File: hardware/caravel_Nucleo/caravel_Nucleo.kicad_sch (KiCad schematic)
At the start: 88 parts, among them J1 USB4105-GF-A, J10 PinHeader_1x11, J11 PinHeader_1x02, J12 PinHeader_1x02, J2 M20-9990246, J3 PinHeader_1x02, J4 61300411121, J5 PinHeader_1x02, J6 PinHeader_1x02, J7 61300611121, J8 640456-3, J9 640456-3, Q1 BSS84AKW, SW1 KMR2, T1 Logo, T2 Logo, U1 FT232HQ, U12 NUCLEO144-F429ZI, U2 SN74LVC1G125DCKR, U3 SN74LVC1G125DCKR, U4 MAX811REUS+T, U5 MCP4661-103E/ML, U6 Caravel_breakout_PCB, U7 W25Q32FVSS, U9 MIC2211-AAYML-TR, X1 ECS-2520MVLC-100-BN-TR, Y1 ABM8G-12.000MHZ-18-D2Y-T

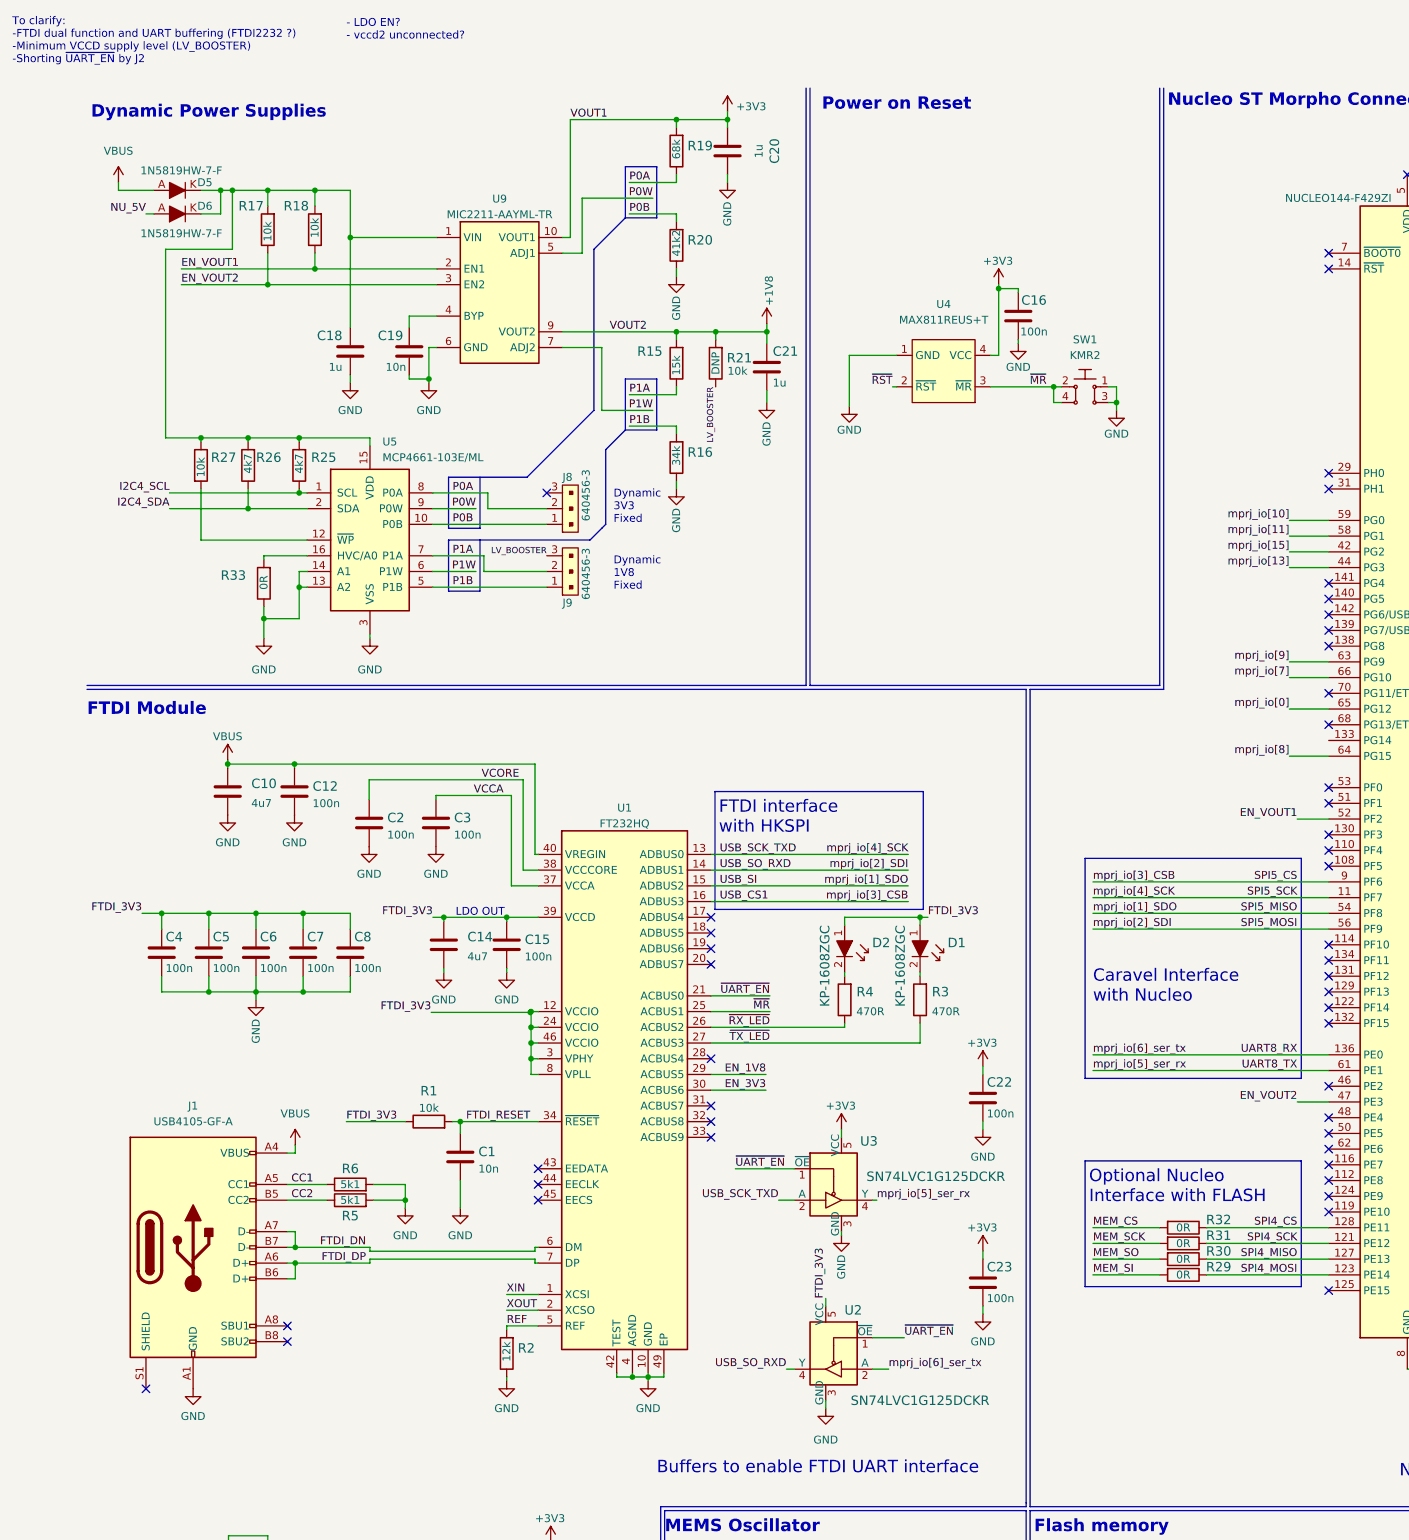
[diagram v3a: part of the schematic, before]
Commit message: Add UART_EN signal short protection for FTDI, add OR gate for enabling LDO
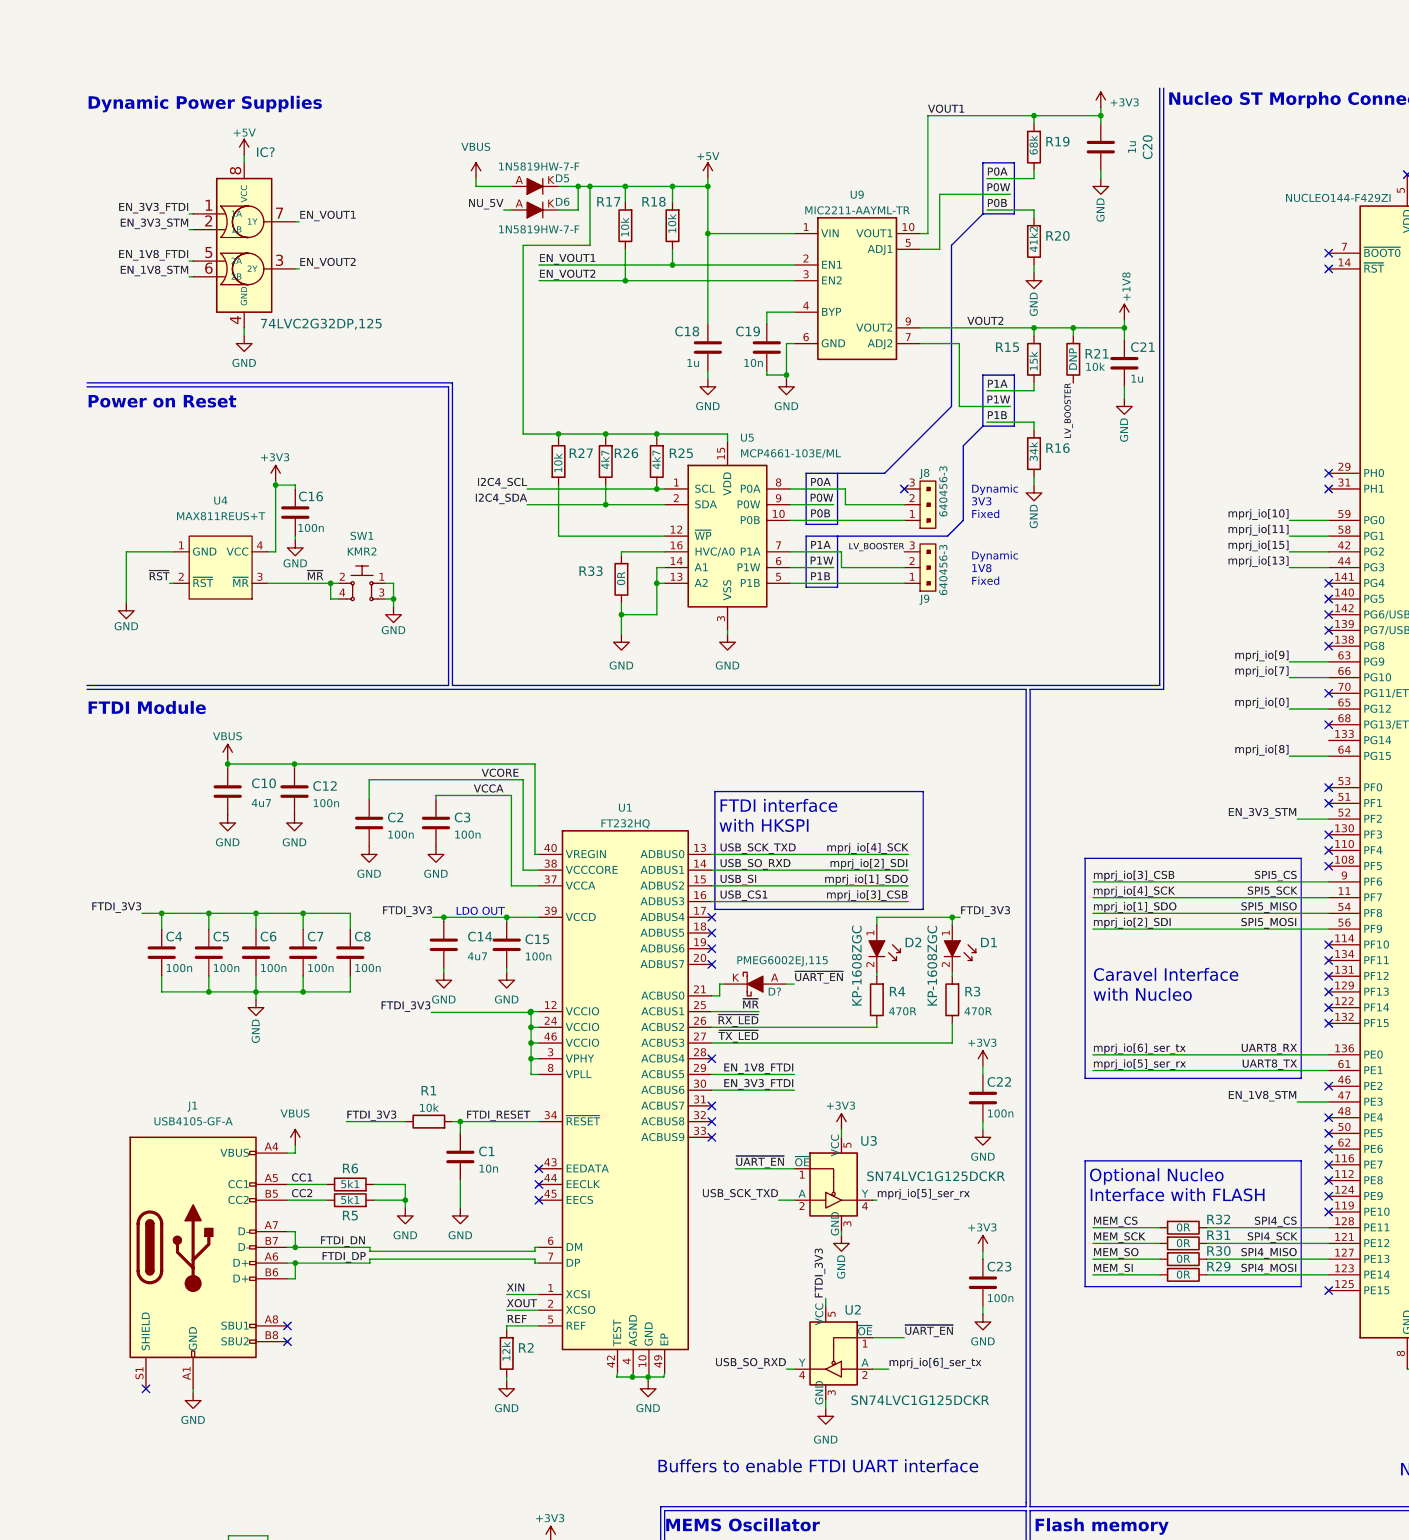
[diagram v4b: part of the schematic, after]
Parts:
- added D?: PMEG6002EJ,115, antmicro-footprints:SOD-323F, symbol antmicroDiodesRectifiersSingle:PMEG6002EJ,115
- added IC?: 74LVC2G32DP,125, antmicro-footprints:TSSOP-8_W3mm, symbol antmicroLogicGatesandInverters:74LVC2G32DP,125
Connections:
- net +5V: now also C18.1, D5.K, D6.K, R17.2, R18.2, R25.2, R26.2, R27.1, U5.15 (VDD), U9.1 (VIN), IC?.8 (VCC)
- net AGND: now also IC?.4 (GND)
- net EN_VOUT1: now also IC?.7 (1Y); no longer U12.52 (PF2)
- net EN_VOUT2: now also IC?.3 (2Y); no longer U12.47 (PE3)
- net ~{UART_EN}: now also D?.A; no longer U1.21 (ACBUS0)
- net EN_1V8 renamed EN_1V8_FTDI
- net EN_1V8_FTDI: now also IC?.5 (2A)
- net EN_3V3 renamed EN_3V3_FTDI
- net EN_3V3_FTDI: now also IC?.1 (1A)
- new net: D?.K, U1.21 (ACBUS0)
- new net EN_1V8_STM: IC?.6 (2B), U12.47 (PE3)
- new net EN_3V3_STM: IC?.2 (1B), U12.52 (PF2)
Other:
- note removed: "- LDO EN? - vccd2 unconnected?"
- note removed: "To clarify: -FTDI dual function and UART buffering (FTDI2232 ?) -Minimum VCCD supply level (LV_BOOSTER) -Shorting ~{UART_EN} by J2"
- moved on the sheet: C16, C18, C19, C20, C21, D1, D2, D5, D6, J8, J9, R15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

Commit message: Add missing decoupling, fix passive components size
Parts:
- removed R16: R_34k_0402, antmicro-footprints:0402-res, symbol antmicroResistors0402:R_34k_0402
- removed R23: R_10k_0402, antmicro-footprints:0402-res, symbol antmicroResistors0402:R_10k_0402
- removed TP1: TP_SMD1MM, antmicro-footprints:Testpoint_smd_1mm, symbol antmicroTestPoints:TP_SMD1MM
- added C24, C25, C26, C27, C28, C29, C30, C31, C32: C_100n_0603, antmicro-footprints:0603-cap, symbol antmicroCapacitors0603:C_100n_0603
- added C33: C_1u_0603, antmicro-footprints:0603-cap, symbol antmicroCapacitors0603:C_1u_0603
- added J13: PinHeader_1x02, antmicro-footprints:PinHeader_1x2_P2.54mm, symbol antmicroRectangularConnectorsHeadersMalePins:PinHeader_1x02
- added R16: R_34k_0603, antmicro-footprints:0603-res, symbol antmicroResistors0603:R_34k_0603
- added R23: R_10k_0603, antmicro-footprints:0603-res, symbol antmicroResistors0603:R_10k_0603
- gave numbers to parts that had none: 2
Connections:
- net +1V8: now also C26.2, C28.2, C30.2
- net +3V3: now also C24.2, C25.2, C27.2
- net +5V: now also C33.1
- net AGND: now also C24.1, C25.1, C26.1, C27.1, C28.1, C29.1, C30.1, C31.1, C32.1, C33.2, J13.1, J13.2, R16.1
- net FTDI_3V3: now also U1.12 (VCCIO), U1.24 (VCCIO), U1.3 (VPHY), U1.46 (VCCIO), U1.8 (VPLL)
- net P1B: now also R16.2
- net gpio: now also R23.2
- net vccd2: now also C32.2
- net vdda1: now also C29.2
- net vdda2: now also C31.2
- net at Q1.1 (G): now also R23.1

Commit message: Add on schematic I2C logic level translator, add missing decoupling, change J12 voltage assigment
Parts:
- removed C33: C_1u_0603, antmicro-footprints:0603-cap, symbol antmicroCapacitors0603:C_1u_0603
- removed J2: M20-9990246, antmicro-footprints:PinHeader_1x2_P2.54mm, symbol antmicroRectangularConnectorsHeadersMalePins:M20-9990246
- added C33, C34, C35, C36: C_100n_0603, antmicro-footprints:0603-cap, symbol antmicroCapacitors0603:C_100n_0603
- added J2: PinHeader_1x02, antmicro-footprints:PinHeader_1x2_P2.54mm, symbol antmicroRectangularConnectorsHeadersMalePins:PinHeader_1x02
- added R24, R28: R_4k7_0603, antmicro-footprints:0603-res, symbol antmicroResistors0603:R_4k7_0603
- added U8: NTS0102DP, antmicro-footprints:TSSOP-8_W3mm, symbol antmicroLogicTranslatorsLevelShifters:NTS0102DP
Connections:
- net +3V3: no longer C23.1
- net +5V: now also C33.1, C34.1, C36.1, U8.7 (VCC_B); no longer J12.1
- net AGND: now also C33.2, C34.2, C35.2, C36.2, J2.2, U8.2 (GND)
- net FTDI_3V3: now also C23.1
- net I2C4_SCL: now also U8.8 (B1); no longer U12.115 (PD12)
- net I2C4_SDA: now also U8.1 (B2); no longer U12.113 (PD13)
- net NU_5V: no longer D6.A
- net ~{UART_EN}: now also J2.1
- net NU_3V3: now reaches U12.16 (+3V3)
- net NU_3V3: now also C35.1, R24.2, R28.2, U8.3 (VCC_A), U8.6 (OE)
- new net I2C4_SCL_3V3: R24.1, U12.115 (PD12), U8.5 (A1)
- new net I2C4_SDA_3V3: R28.1, U12.113 (PD13), U8.4 (A2)
- new net NU_5V_JMPR: D6.A, J12.1
- no-connect marks 90 -> 89
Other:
- note added: "1V8"
- note added: "3V3"
- note added: "Dynamic Fixed"
- note removed: "Dynamic 1V8 Fixed"
- note removed: "Dynamic 3V3 Fixed"
- moved on the sheet: C16, C24, C25, C26, C27, C28, C29, C30, C31, C32, IC1, J10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
